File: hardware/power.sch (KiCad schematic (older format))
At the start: 79 parts, among them CON2 BARREL_JACK, U18 TPS5420D, U19 TPS5420D, U20 LP5907-3.0, U21 LP2985A-10DBVR, U22 TPS560200, U23 TPS7A91, U24 TPS7A91, U25 TPS7A7001DDA, U32 TPS7A91

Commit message: Fixed ERC errors.
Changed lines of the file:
@@
 	1    0    0    -1
 $EndComp
-Text HLabel 12800 4950 2    60   Output ~ 0
-1V8
-Text HLabel 13300 2000 2    60   Output ~ 0
-3V3A
 $Comp
 L Device:LED D1
@@
 Text Label 9750 7950 2    60   ~ 0
 3V6
-Text HLabel 11650 7950 2    60   Output ~ 0
-3V0
 $Comp
 L Regulator_Linear:LP2985-10.0 U21
@@
 	1    0    0    -1
 $EndComp
-Text HLabel 6250 3550 2    60   Output ~ 0
-10V
 $Comp
 L Device:C C95
@@
 Wire Wire Line
 	9650 2000 9650 2100
-Connection ~ 9650 2000
 Wire Wire Line
 	9650 2250 9800 2250
 Connection ~ 9050 2000
 Wire Wire Line
-	11100 2000 11200 2000
-Wire Wire Line
 	11100 2100 11200 2100
 Wire Wire Line
 	11200 2100 11200 2000
-Connection ~ 11200 2000
 Wire Wire Line
 	11800 2350 11800 2400
@@
 	8950 4950 9000 4950
 Wire Wire Line
-	9750 5050 9600 5050
-Connection ~ 9600 4950
-Wire Wire Line
 	9600 5200 9750 5200
 Connection ~ 9000 4950
 Wire Wire Line
-	11050 4950 11150 4950
-Wire Wire Line
 	11050 5050 11150 5050
 Wire Wire Line
 	11150 5050 11150 4950
-Connection ~ 11150 4950
 Connection ~ 12500 4950
 Wire Wire Line
@@
 	11400 5300 11400 5350
 Connection ~ 11400 5350
-Wire Wire Line
-	9600 5050 9600 4950
 Connection ~ 9650 2100
 Wire Wire Line
@@
 	5650 2150 5900 2150
 Wire Wire Line
-	6150 2150 6400 2150
+	6150 2150 6250 2150
 Wire Wire Line
 	10050 7950 10150 7950
@@
 	4100 3550 4450 3550
 Wire Wire Line
-	6150 3550 6250 3550
-Wire Wire Line
-	9650 2000 9800 2000
-Wire Wire Line
 	9050 2000 9250 2000
 Wire Wire Line
@@
 	11450 2400 11800 2400
 Wire Wire Line
-	9600 4950 9750 4950
-Wire Wire Line
 	9000 4950 9200 4950
 Wire Wire Line
@@
 Wire Wire Line
 	11750 5350 11750 5400
-Wire Wire Line
-	9200 4950 9600 4950
 Wire Wire Line
 	11400 5350 11750 5350
@@
 $EndComp
 Wire Wire Line
-	6200 4750 7100 4750
+	6200 4750 6800 4750
 Wire Wire Line
 	7100 4850 7100 4750
@@
 	1    0    0    -1
 $EndComp
-Text Label 7600 6150 0    60   ~ 0
-3V6
 Wire Wire Line
 	5850 6150 6200 6150
@@
 $EndComp
 Wire Wire Line
-	6200 6150 7100 6150
+	6200 6150 6800 6150
 Wire Wire Line
 	7100 6250 7100 6150
@@
 	4450 3650 4450 3550
 Wire Wire Line
-	5500 3550 6150 3550
-Wire Wire Line
 	5500 3650 5800 3650
 Wire Wire Line
@@
 Connection ~ 6300 7850
 Wire Wire Line
-	6300 7850 7200 7850
+	6300 7850 6800 7850
 Wire Wire Line
 	6300 8350 6650 8350
@@
 $EndComp
 NoConn ~ 3900 8050
-Text HLabel 7700 7850 2    60   Output ~ 0
-1V0
 $Comp
 L Device:L_Core_Ferrite L6
@@
 	10400 4050 10400 3950
 Connection ~ 10400 4050
-Text HLabel 12600 3550 2    60   Output ~ 0
-5V
 Wire Wire Line
 	12250 5350 12250 5450
@@
 Wire Wire Line
 	11050 6150 11200 6150
-Text HLabel 14800 6350 2    60   Output ~ 0
-3V3D
 $Comp
 L fmcw-rescue:TPS7A91-fmcw3-rescue U32
@@
 Wire Wire Line
 	11150 6350 11150 6450
-Connection ~ 11150 6350
 Connection ~ 10550 6350
-Wire Wire Line
-	12600 6350 12700 6350
 Connection ~ 14200 6350
 Wire Wire Line
@@
 Wire Wire Line
 	12700 6450 12700 6350
-Connection ~ 12700 6350
 Wire Wire Line
 	13300 6700 13300 6750
@@
 Connection ~ 12950 6750
 Wire Wire Line
-	11150 6350 11300 6350
-Wire Wire Line
 	10550 6350 10750 6350
 Wire Wire Line
@@
 Wire Wire Line
 	9850 7950 10050 7950
+Text HLabel 7600 6150 2    60   Output ~ 0
+3V6
+Wire Wire Line
+	9200 4950 9600 4950
+Wire Wire Line
+	9750 5050 9600 5050
+Wire Wire Line
+	9600 5050 9600 4950
+Text HLabel 11650 7950 2    60   Output ~ 0
+3V0
+Wire Wire Line
+	5500 3550 6150 3550
+Wire Wire Line
+	6150 3550 6250 3550
+Text HLabel 6250 3550 2    60   Output ~ 0
+10V
+Text HLabel 7700 7850 2    60   Output ~ 0
+1V0
+Text HLabel 12800 4950 2    60   Output ~ 0
+1V8
+Text HLabel 12600 3550 2    60   Output ~ 0
+5V
+Text HLabel 13300 2000 2    60   Output ~ 0
+3V3A
+Text HLabel 14800 6350 2    60   Output ~ 0
+3V3D
+$Comp
+L power:PWR_FLAG #FLG0115
+U 1 1 5CF39927
+P 6800 6150
+F 0 "#FLG0115" H 6800 6225 50  0001 C CNN
+F 1 "PWR_FLAG" H 6800 6324 50  0000 C CNN
+F 2 "" H 6800 6150 50  0001 C CNN
+F 3 "~" H 6800 6150 50  0001 C CNN
+	1    6800 6150
+	1    0    0    -1
+$EndComp
+Connection ~ 6800 6150
+Wire Wire Line
+	6800 6150 7100 6150
+$Comp
+L power:PWR_FLAG #FLG0116
+U 1 1 5CF399D9
+P 6800 4750
+F 0 "#FLG0116" H 6800 4825 50  0001 C CNN
+F 1 "PWR_FLAG" H 6800 4924 50  0000 C CNN
+F 2 "" H 6800 4750 50  0001 C CNN
+F 3 "~" H 6800 4750 50  0001 C CNN
+	1    6800 4750
+	1    0    0    -1
+$EndComp
+Connection ~ 6800 4750
+Wire Wire Line
+	6800 4750 7100 4750
+$Comp
+L power:PWR_FLAG #FLG0117
+U 1 1 5CF39A84
+P 6800 7850
+F 0 "#FLG0117" H 6800 7925 50  0001 C CNN
+F 1 "PWR_FLAG" H 6800 8024 50  0000 C CNN
+F 2 "" H 6800 7850 50  0001 C CNN
+F 3 "~" H 6800 7850 50  0001 C CNN
+	1    6800 7850
+	1    0    0    -1
+$EndComp
+Connection ~ 6800 7850
+Wire Wire Line
+	6800 7850 7200 7850
+$Comp
+L power:PWR_FLAG #FLG0119
+U 1 1 5CF3F318
+P 6250 2150
+F 0 "#FLG0119" H 6250 2225 50  0001 C CNN
+F 1 "PWR_FLAG" H 6250 2324 50  0000 C CNN
+F 2 "" H 6250 2150 50  0001 C CNN
+F 3 "~" H 6250 2150 50  0001 C CNN
+	1    6250 2150
+	1    0    0    -1
+$EndComp
+Connection ~ 6250 2150
+Wire Wire Line
+	6250 2150 6400 2150
 $EndSCHEMATC

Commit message: Improved documentation and added schematics to default libraries.
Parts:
- U20: symbol fmcw-rescue:LP5907-fmcw3-rescue -> Regulator_Linear:LP5907MFX-3.0
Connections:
- net GND: no longer U20.2 (GND)
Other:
- moved on the sheet: C172, C85, C93, U20
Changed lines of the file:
@@
 5V6
 $Comp
-L fmcw-rescue:LP5907-fmcw3-rescue U20
+L Regulator_Linear:LP5907MFX-3.0 U20
 U 1 1 596BD518
 P 10650 8000
-F 0 "U20" H 10650 8337 60  0000 C CNN
-F 1 "LP5907-3.0" H 10650 8231 60  0000 C CNN
+F 0 "U20" H 10650 8389 60  0000 C CNN
+F 1 "LP5907-3.0" H 10650 8283 60  0000 C CNN
 F 2 "Package_TO_SOT_SMD:SOT-23-5" H 10650 8050 60  0001 C CNN
 F 3 "" H 10650 8050 60  0000 C CNN
@@
 L Device:C C93
 U 1 1 596BD876
-P 11250 8200
-F 0 "C93" H 11275 8300 50  0000 L CNN
-F 1 "10u" H 11275 8100 50  0000 L CNN
-F 2 "Capacitor_SMD:C_0805_2012Metric" H 11288 8050 30  0001 C CNN
-F 3 "" H 11250 8200 60  0000 C CNN
-F 4 "CL21B106KQQNNNE" H 1000 1350 50  0001 C CNN "MFN"
-	1    11250 8200
+P 11050 8150
+F 0 "C93" H 11075 8250 50  0000 L CNN
+F 1 "10u" H 11075 8050 50  0000 L CNN
+F 2 "Capacitor_SMD:C_0805_2012Metric" H 11088 8000 30  0001 C CNN
+F 3 "" H 11050 8150 60  0000 C CNN
+F 4 "CL21B106KQQNNNE" H 800 1300 50  0001 C CNN "MFN"
+	1    11050 8150
 	1    0    0    -1
 $EndComp
@@
 L power:GND #PWR0179
 U 1 1 596BD9CD
-P 11250 8450
-F 0 "#PWR0179" H 11250 8200 50  0001 C CNN
-F 1 "GND" H 11250 8300 50  0000 C CNN
-F 2 "" H 11250 8450 60  0000 C CNN
-F 3 "" H 11250 8450 60  0000 C CNN
-	1    11250 8450
+P 11050 8400
+F 0 "#PWR0179" H 11050 8150 50  0001 C CNN
+F 1 "GND" H 11050 8250 50  0000 C CNN
+F 2 "" H 11050 8400 60  0000 C CNN
+F 3 "" H 11050 8400 60  0000 C CNN
+	1    11050 8400
 	1    0    0    -1
 $EndComp
@@
 L Device:C C85
 U 1 1 596BDC48
-P 9850 8200
-F 0 "C85" H 9875 8300 50  0000 L CNN
-F 1 "10u" H 9875 8100 50  0000 L CNN
-F 2 "Capacitor_SMD:C_0805_2012Metric" H 9888 8050 30  0001 C CNN
-F 3 "" H 9850 8200 60  0000 C CNN
-F 4 "CL21B106KQQNNNE" H 1000 1550 50  0001 C CNN "MFN"
-	1    9850 8200
+P 10050 8150
+F 0 "C85" H 10075 8250 50  0000 L CNN
+F 1 "10u" H 10075 8050 50  0000 L CNN
+F 2 "Capacitor_SMD:C_0805_2012Metric" H 10088 8000 30  0001 C CNN
+F 3 "" H 10050 8150 60  0000 C CNN
+F 4 "CL21B106KQQNNNE" H 1200 1500 50  0001 C CNN "MFN"
+	1    10050 8150
 	1    0    0    -1
 $EndComp
@@
 L power:GND #PWR0180
 U 1 1 596BDD85
-P 9850 8400
-F 0 "#PWR0180" H 9850 8150 50  0001 C CNN
-F 1 "GND" H 9850 8250 50  0000 C CNN
-F 2 "" H 9850 8400 60  0000 C CNN
-F 3 "" H 9850 8400 60  0000 C CNN
-	1    9850 8400
-	1    0    0    -1
-$EndComp
-Text Label 9750 7950 2    60   ~ 0
+P 10050 8350
+F 0 "#PWR0180" H 10050 8100 50  0001 C CNN
+F 1 "GND" H 10050 8200 50  0000 C CNN
+F 2 "" H 10050 8350 60  0000 C CNN
+F 3 "" H 10050 8350 60  0000 C CNN
+	1    10050 8350
+	1    0    0    -1
+$EndComp
+Text Label 9950 7900 2    60   ~ 0
 3V6
 $Comp
@@
 L Device:C C172
 U 1 1 59759EF1
-P 11450 8200
-F 0 "C172" H 11475 8300 50  0000 L CNN
-F 1 "DNP" H 11475 8100 50  0000 L CNN
-F 2 "Capacitor_SMD:C_0805_2012Metric" H 11488 8050 30  0001 C CNN
-F 3 "" H 11450 8200 60  0000 C CNN
-	1    11450 8200
+P 11250 8150
+F 0 "C172" H 11275 8250 50  0000 L CNN
+F 1 "DNP" H 11275 8050 50  0000 L CNN
+F 2 "Capacitor_SMD:C_0805_2012Metric" H 11288 8000 30  0001 C CNN
+F 3 "" H 11250 8150 60  0000 C CNN
+	1    11250 8150
 	1    0    0    -1
 $EndComp
@@
 L power:GND #PWR0219
 U 1 1 5975A119
-P 11450 8450
-F 0 "#PWR0219" H 11450 8200 50  0001 C CNN
-F 1 "GND" H 11450 8300 50  0000 C CNN
-F 2 "" H 11450 8450 60  0000 C CNN
-F 3 "" H 11450 8450 60  0000 C CNN
-	1    11450 8450
+P 11250 8400
+F 0 "#PWR0219" H 11250 8150 50  0001 C CNN
+F 1 "GND" H 11250 8250 50  0000 C CNN
+F 2 "" H 11250 8400 60  0000 C CNN
+F 3 "" H 11250 8400 60  0000 C CNN
+	1    11250 8400
 	1    0    0    -1
 $EndComp
@@
 	10650 8350 10650 8400
 Wire Wire Line
-	10150 8050 10050 8050
-Wire Wire Line
-	10050 8050 10050 7950
-Connection ~ 10050 7950
-Wire Wire Line
-	9850 8350 9850 8400
+	10350 8000 10250 8000
+Wire Wire Line
+	10250 8000 10250 7900
+Connection ~ 10250 7900
+Wire Wire Line
+	10050 8300 10050 8350
 Wire Wire Line
 	4050 3550 4100 3550
@@
 	6150 2150 6250 2150
 Wire Wire Line
-	10050 7950 10150 7950
+	10250 7900 10350 7900
 Wire Wire Line
 	4100 3550 4450 3550
@@
 	1    0    0    -1
 $EndComp
-Wire Wire Line
-	6650 8350 6650 9200
-Wire Wire Line
-	6650 9200 4600 9200
-Wire Wire Line
-	4600 8050 4600 9200
-Wire Wire Line
-	6300 8250 6300 8350
-Connection ~ 6300 8350
-Wire Wire Line
-	6300 8350 6300 8450
 Connection ~ 6300 7850
 Wire Wire Line
 	6300 7850 6800 7850
-Wire Wire Line
-	6300 8350 6650 8350
 $Comp
 L power:GND #PWR0195
@@
 	14200 6850 14200 6750
 Wire Wire Line
-	11150 7950 11250 7950
-Wire Wire Line
-	11250 8050 11250 7950
-Connection ~ 11250 7950
-Wire Wire Line
-	11250 7950 11450 7950
-Wire Wire Line
-	11450 7950 11450 8050
-Connection ~ 11450 7950
-Wire Wire Line
-	11450 7950 11650 7950
-Wire Wire Line
-	11450 8450 11450 8350
-Wire Wire Line
-	11250 8450 11250 8350
-Wire Wire Line
-	9750 7950 9850 7950
-Wire Wire Line
-	9850 8050 9850 7950
-Connection ~ 9850 7950
-Wire Wire Line
-	9850 7950 10050 7950
+	10950 7900 11050 7900
+Wire Wire Line
+	11050 8000 11050 7900
+Connection ~ 11050 7900
+Wire Wire Line
+	11050 7900 11250 7900
+Wire Wire Line
+	11250 7900 11250 8000
+Connection ~ 11250 7900
+Wire Wire Line
+	11250 7900 11450 7900
+Wire Wire Line
+	11250 8400 11250 8300
+Wire Wire Line
+	11050 8400 11050 8300
+Wire Wire Line
+	9950 7900 10050 7900
+Wire Wire Line
+	10050 8000 10050 7900
+Connection ~ 10050 7900
+Wire Wire Line
+	10050 7900 10250 7900
 Text HLabel 7600 6150 2    60   Output ~ 0
 3V6
@@
 Wire Wire Line
 	9600 5050 9600 4950
-Text HLabel 11650 7950 2    60   Output ~ 0
+Text HLabel 11450 7900 2    60   Output ~ 0
 3V0
 Wire Wire Line
@@
 Wire Wire Line
 	6250 2150 6400 2150
+Wire Wire Line
+	6300 8250 6300 8350
+Wire Wire Line
+	6300 8350 6100 8350
+Wire Wire Line
+	6100 8350 6100 8700
+Wire Wire Line
+	6100 8700 4600 8700
+Wire Wire Line
+	4600 8700 4600 8050
+Connection ~ 6300 8350
+Wire Wire Line
+	6300 8350 6300 8450
 $EndSCHEMATC

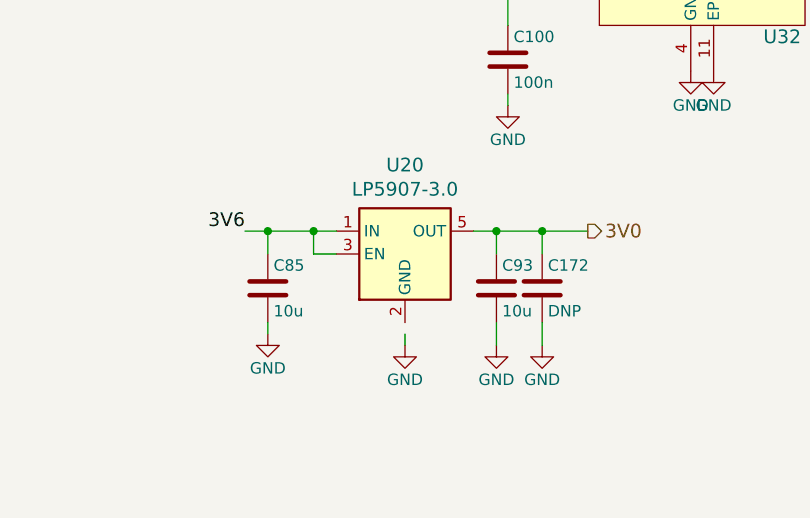
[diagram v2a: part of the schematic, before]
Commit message: Improved documentation and parts of the schematic.
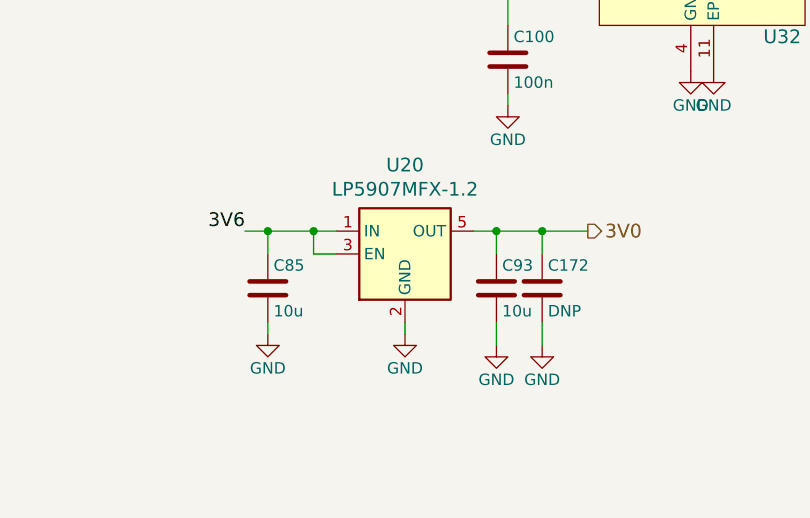
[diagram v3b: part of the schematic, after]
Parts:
- U20: value LP5907-3.0 -> LP5907MFX-1.2
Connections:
- net GND: now also U20.2 (GND)
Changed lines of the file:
@@
 P 10650 8000
 F 0 "U20" H 10650 8389 60  0000 C CNN
-F 1 "LP5907-3.0" H 10650 8283 60  0000 C CNN
+F 1 "LP5907MFX-1.2" H 10650 8283 60  0000 C CNN
 F 2 "Package_TO_SOT_SMD:SOT-23-5" H 10650 8050 60  0001 C CNN
 F 3 "" H 10650 8050 60  0000 C CNN
@@
 L power:GND #PWR0178
 U 1 1 596BD741
-P 10650 8400
-F 0 "#PWR0178" H 10650 8150 50  0001 C CNN
-F 1 "GND" H 10650 8250 50  0000 C CNN
-F 2 "" H 10650 8400 60  0000 C CNN
-F 3 "" H 10650 8400 60  0000 C CNN
-	1    10650 8400
+P 10650 8350
+F 0 "#PWR0178" H 10650 8100 50  0001 C CNN
+F 1 "GND" H 10650 8200 50  0000 C CNN
+F 2 "" H 10650 8350 60  0000 C CNN
+F 3 "" H 10650 8350 60  0000 C CNN
+	1    10650 8350
 	1    0    0    -1
 $EndComp
@@
 	2750 1950 2750 2100
 Wire Wire Line
-	10650 8350 10650 8400
+	10650 8300 10650 8350
 Wire Wire Line
 	10350 8000 10250 8000

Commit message: Changed components to official libs.
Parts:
- U23, U24, U32: footprint fmcw:SON-10_2.5x2.5mm -> Package_DFN_QFN:DFN-10-1EP_2.5x2.5mm_P0.5mm_EP1.2x2mm; symbol fmcw-rescue:TPS7A91-fmcw3-rescue -> Regulator_Linear:TPS7A91
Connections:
- wire segments 276 -> 275
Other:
- moved on the sheet: C100, C169, C175, C219, C91, C92, R32, R33

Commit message: Finished design, began routing.
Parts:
- C176: renamed from C82; footprint Capacitor_SMD:C_0805_2012Metric -> Capacitor_SMD:C_0402_1005Metric
- CON1: renamed from CON2; footprint fmcw:EJ508A -> Connector_BarrelJack:BarrelJack_Wuerth_6941xx301002; MFN EJ508A -> 694108301002
- D3: footprint Diode_SMD:D_SOD-123F -> fmcw:SOD-123F
- D4: renamed from D2; footprint Diode_SMD:D_SOD-123F -> fmcw:SOD-123F
- U33: renamed from U20; value LP5907MFX-1.2 -> LP5907MFX-3.0
- renumbered C62 to C169, C69 to C170, C74 to C171, C73 to C172, C81 to C173, C76 to C174, C75 to C175, C89 to C177, C64 to C178, C78 to C179, C77 to C180, C83 to C181, C70 to C182, C84 to C183, C95 to C184, C71 to C185, C72 to C186, C98 to C187, C177 to C188, C178 to C189, C80 to C190, C79 to C191, C86 to C192, C90 to C193, C87 to C194, C88 to C195, C94 to C196, C91 to C197, C92 to C198, C85 to C199, C96 to C200, C93 to C201, C172 to C202, C100 to C203, C97 to C204, C99 to C205, C103 to C206, C101 to C207, C106 to C208, C104 to C209, C102 to C210, C169 to C211, C105 to C212, C175 to C213, C219 to C214, D1 to D2, FB11 to FB15, L6 to L5, L7 to L6, L5 to L7, R24 to R51, R25 to R52, R26 to R53, R14 to R54, R19 to R55, R28 to R56, R29 to R57, R104 to R58, R30 to R59, R31 to R60, R45 to R61, R46 to R62, R47 to R63, R48 to R64, R32 to R65, R33 to R66, U19 to U26, U18 to U27, U22 to U28, U21 to U29, U25 to U30, U23 to U31, U24 to U32, U32 to U34
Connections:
- wire segments 275 -> 269
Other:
- moved on the sheet: C169, C170, C171, C172, C173, C197, C198, C203
